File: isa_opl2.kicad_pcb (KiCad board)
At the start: 2 copper layers, 104.1 x 73.7 mm, 62 parts, among them J1 AUDIO_OUT, P1 IRQ, P2 ADDR, Q1 2N3904, U1 74LS245, U2 74LS138, U3 74LS138, U4 74LS74, U5 74LS04, U6 YM3812, U7 Y3014B, U8 RC4136, U9 LM386

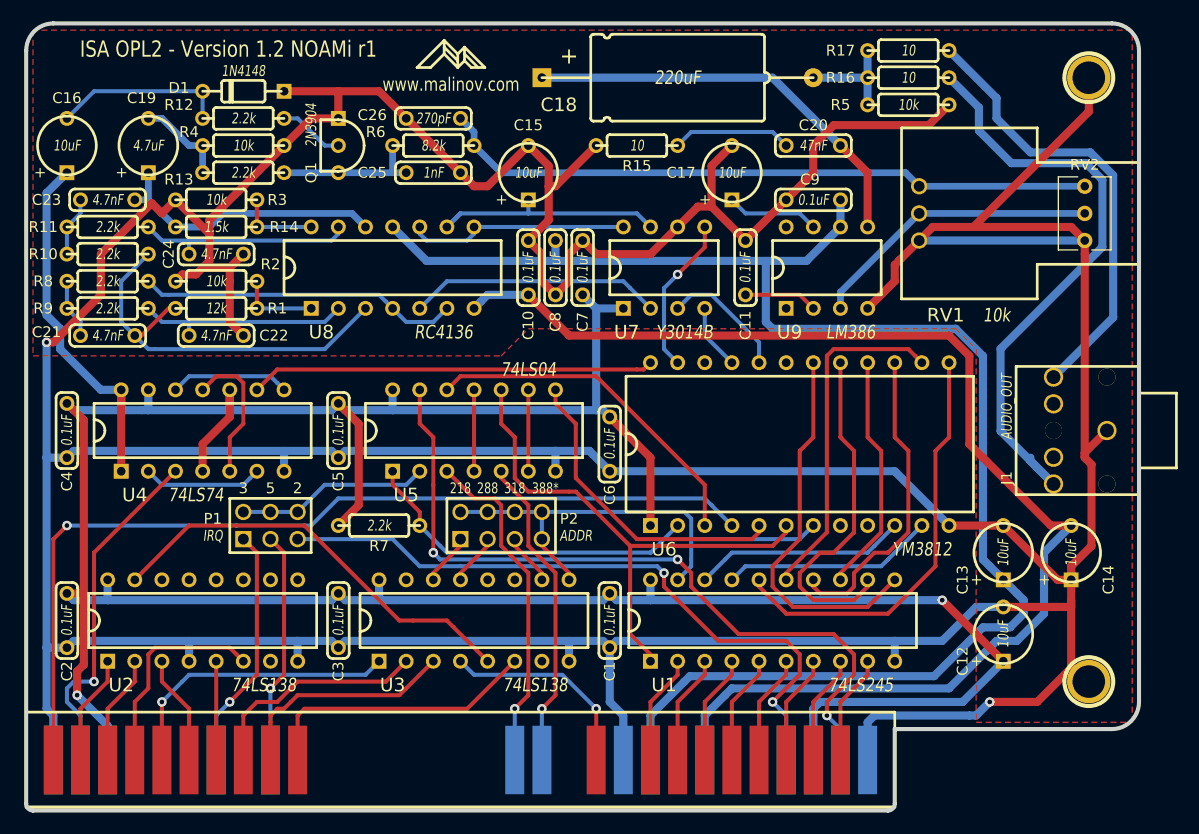
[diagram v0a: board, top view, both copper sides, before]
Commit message: Made connector pads shorter since half of them were not making contact with the connector pins
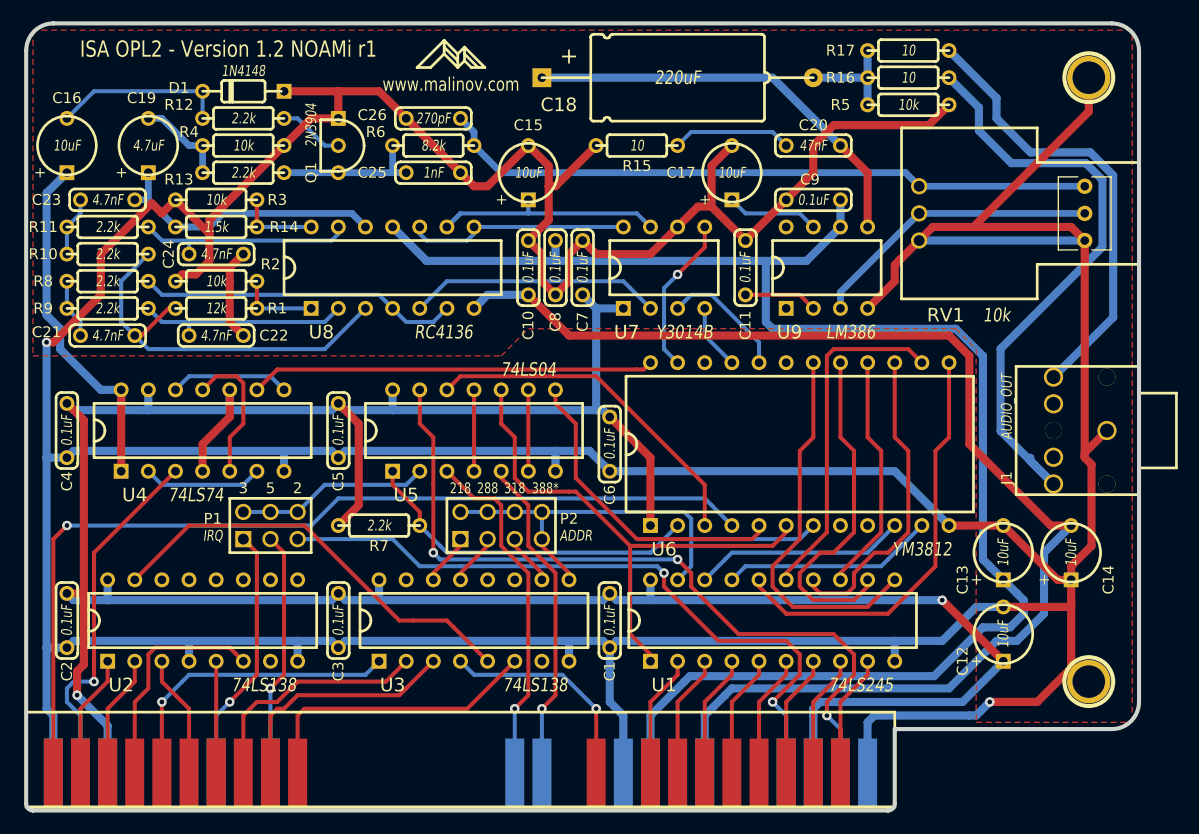
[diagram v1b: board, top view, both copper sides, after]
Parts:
- renumbered RV2 to ?

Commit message: Added service/support info
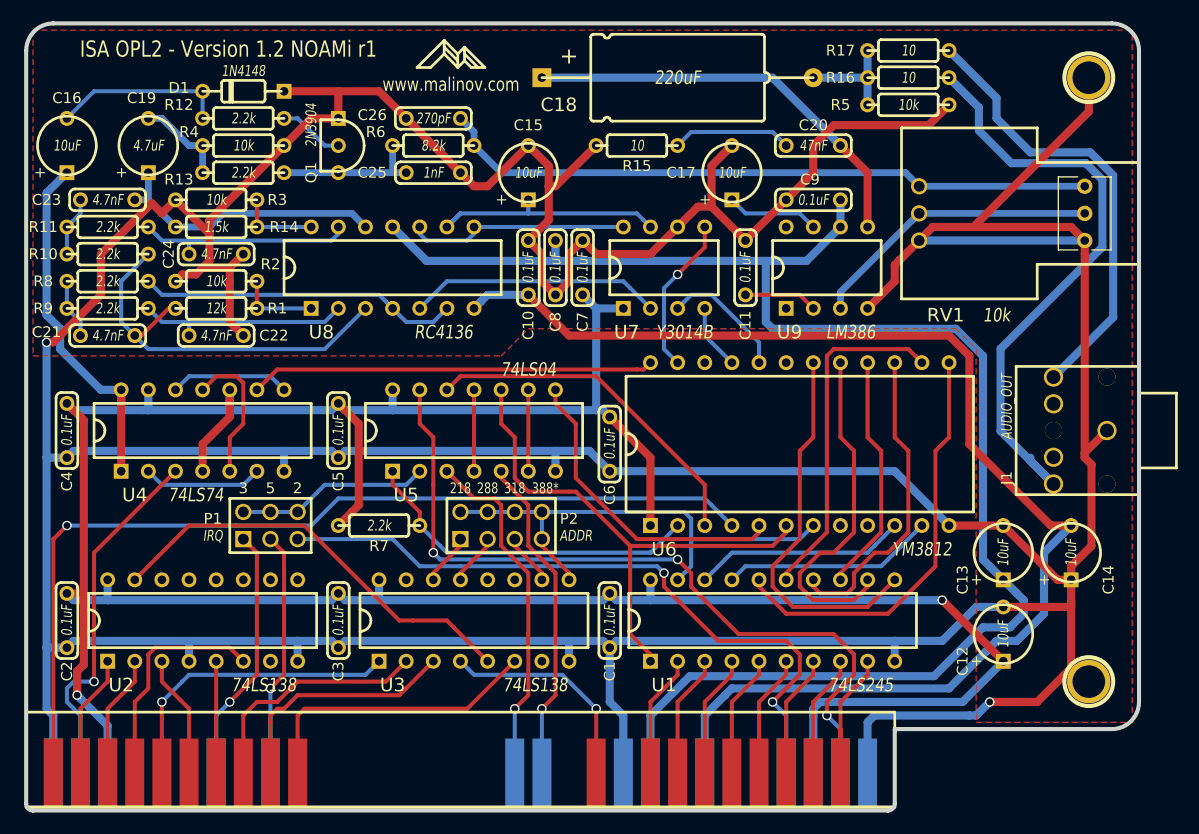
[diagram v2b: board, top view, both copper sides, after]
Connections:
- net /~IOR renamed /~{IOR}
- net /~IOW renamed /~{IOW}
- net /~IRQ renamed /~{IRQ}
- net /~READ renamed /~{READ}
- net /~RESET renamed /~{RESET}
- net /~WRITE renamed /~{WRITE}
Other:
- net class Audio removed
- net class Default removed
- net class Power removed
- net class PwrAudio removed
- board text added: "Service/Support: www.noami.us"
